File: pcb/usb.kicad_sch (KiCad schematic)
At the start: 24 parts, among them J2 USB_C_Receptacle, Q1 FDN340P, Q2 FS8025A, SW2 SW_SPDT, U2 TP4056-42-ESOP8, U3 DW01A

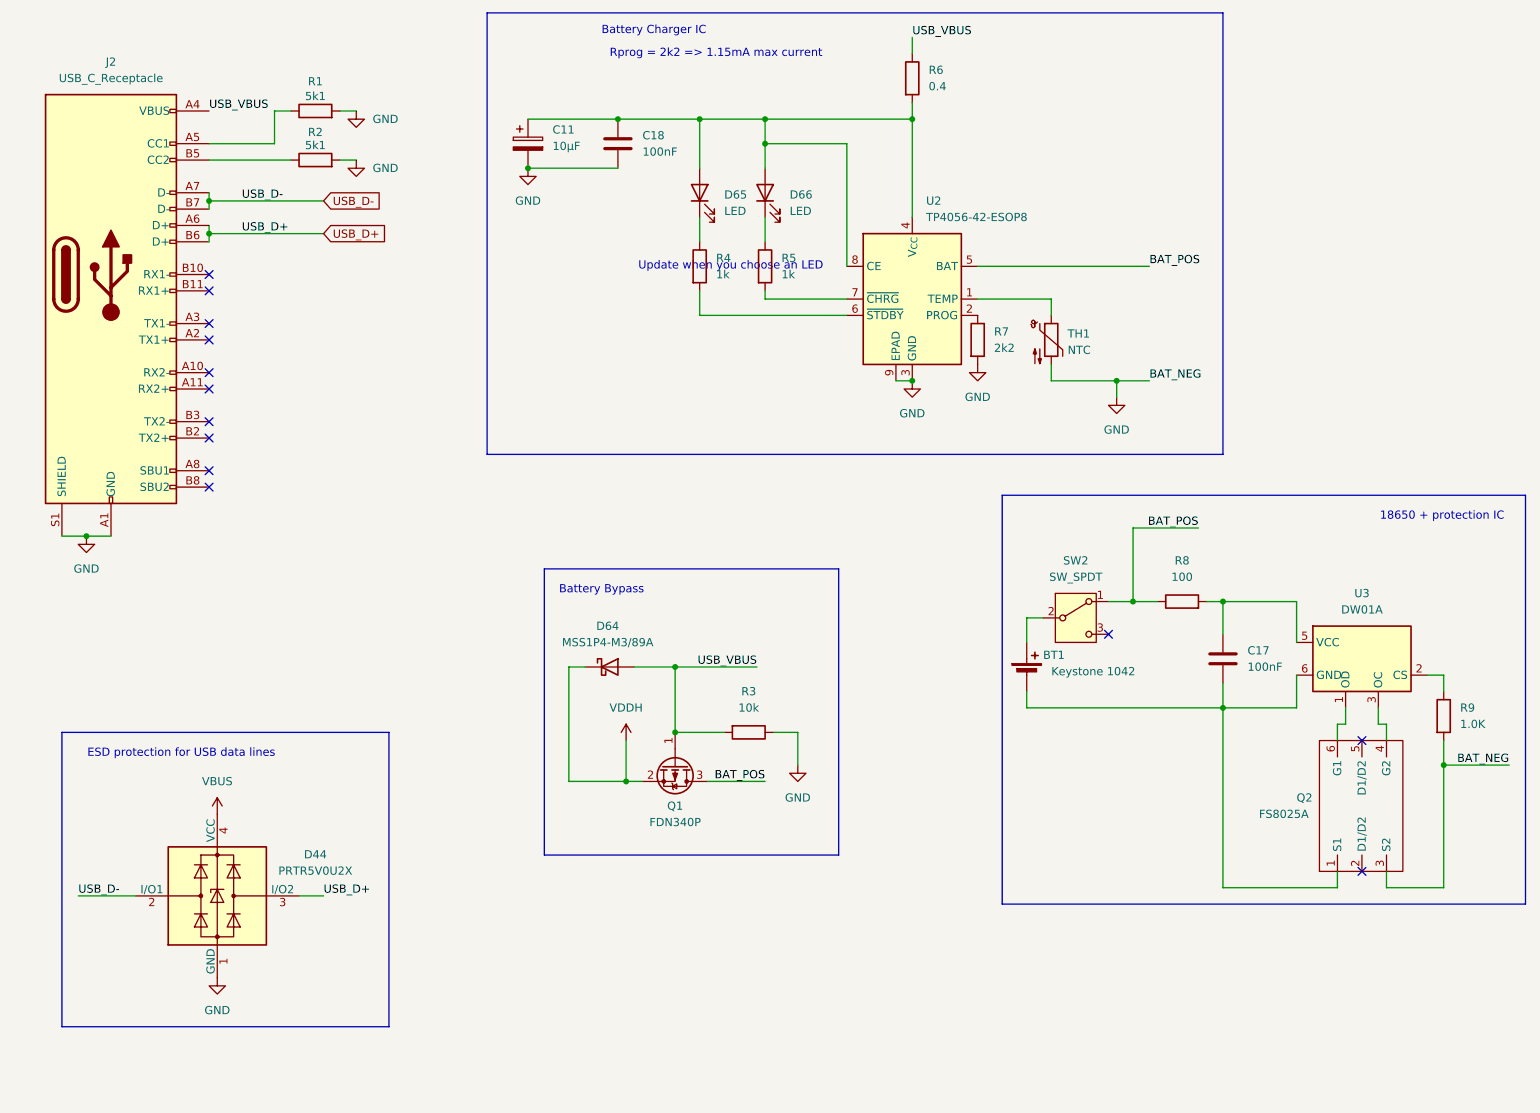
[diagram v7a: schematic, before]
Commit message: Finish power circuitry
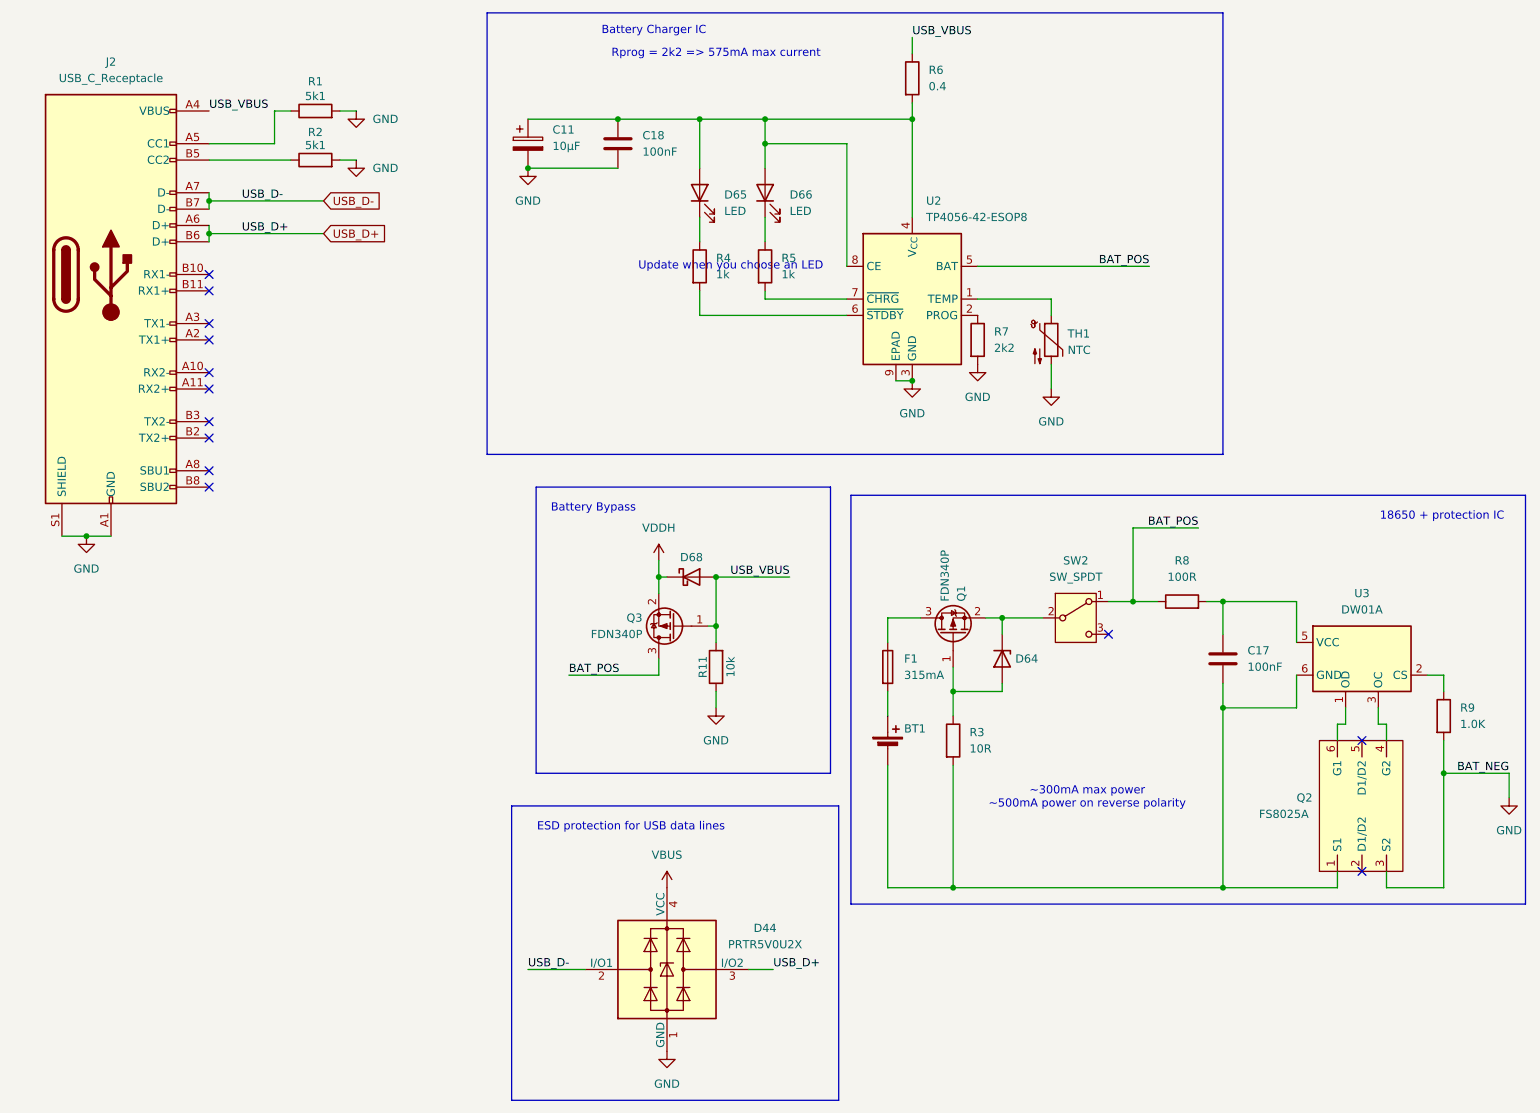
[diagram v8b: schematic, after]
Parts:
- removed D64: MSS1P4-M3/89A, symbol Device:D_Schottky
- added D64: 1SMB5918BT3G, symbol Device:D_Zener
- added D68: MSS1P4-M3/89A, symbol Device:D_Schottky
- added F1: 315mA, symbol Device:Fuse
- added Q3: FDN340P, Package_TO_SOT_SMD:SOT-23, symbol Transistor_FET:FDN340P
- added R11: 10k, Resistor_SMD:R_0805_2012Metric_Pad1.20x1.40mm_HandSolder, symbol Device:R
- R3: value 10k -> 10R; footprint Resistor_SMD:R_0805_2012Metric_Pad1.20x1.40mm_HandSolder -> (none)
- R8: value 100 -> 100R
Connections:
- net BAT_POS: now also Q3.3 (D); no longer Q1.3 (D)
- net GND: now also R11.1; no longer R3.1
- net USB_VBUS: now also D68.2 (A), Q3.1 (G), R11.2; no longer Q1.1 (G), R3.2
- net VDDH: now also D68.1 (K), Q3.2 (S); no longer Q1.2 (S)
- net at BT1.2 (-), C17.2, Q2.1 (S1)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: now also R3.2
- net at SW2.2 (B): now also Q1.2 (S), D64.1 (K); no longer BT1.1 (+)
- new net: D64.2 (A), Q1.1 (G), R3.1
- new net: F1.1, Q1.3 (D)
- new net: BT1.1 (+), F1.2
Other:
- note added: "Rprog = 2k2 => 575mA max current"
- note added: "~300mA max power ~500mA power on reverse polarity"
- note removed: "Rprog = 2k2 => 1.15mA max current"
- moved on the sheet: BT1, D44
